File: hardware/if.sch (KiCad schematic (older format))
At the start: 59 parts, among them U34 ADA4940-2, U35 ADA4940-2

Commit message: Current working version.
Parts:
- C124, C125, C126, C127, C128, C129, C130, C131, C132, C133, C134, C135, C136, C137, C138, C139, C140, C141, C142, C143, C144, C145, C146, C147, C148, C149, C150, C151: footprint fmcw3:C_0402b -> Capacitor_SMD:C_0402_1005Metric; symbol C -> Device:C
- C173: footprint fmcw3:C_0805b -> Capacitor_SMD:C_0805_2012Metric; symbol C -> Device:C
- L10, L11, L8, L9: symbol INDUCTOR_SMALL -> Device:L
- R55, R56, R57, R58, R59, R60, R61, R62, R63, R64, R65, R66, R67, R68, R74, R75, R76, R77, R78, R86, R87, R89, R90, R94: symbol R -> Device:R
- U34, U35: symbol ADA4940-2 -> fmcw3-rescue:ADA4940-2
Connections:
- wire segments 164 -> 217

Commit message: Dropped the 3 from the end of the project name.
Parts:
- L10, L11, L8, L9: footprint fmcw3:C_0805b -> fmcw:C_0805b
- R55, R56, R57, R58, R59, R60, R61, R62, R63, R64, R65, R66, R67, R68, R74, R75, R76, R77, R78, R86, R87, R89, R90, R94: footprint fmcw3:R_0402b -> fmcw:R_0402b
- U34, U35: footprint fmcw3:VFQFN-24 -> fmcw:VFQFN-24; symbol fmcw3-rescue:ADA4940-2 -> fmcw-rescue:ADA4940-2-fmcw3-rescue
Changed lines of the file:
@@
 EESchema Schematic File Version 4
-LIBS:fmcw3-cache
+LIBS:fmcw-cache
 EELAYER 26 0
 EELAYER END
@@
 F 0 "L10" V 1790 1700 50  0000 C CNN
 F 1 "2.2u" V 1699 1700 50  0000 C CNN
-F 2 "fmcw3:C_0805b" H 1600 1700 60  0001 C CNN
+F 2 "fmcw:C_0805b" H 1600 1700 60  0001 C CNN
 F 3 "" H 1600 1700 60  0000 C CNN
 	1    1600 1700
@@
 F 0 "L11" V 1790 2100 50  0000 C CNN
 F 1 "2.2u" V 1699 2100 50  0000 C CNN
-F 2 "fmcw3:C_0805b" H 1600 2100 60  0001 C CNN
+F 2 "fmcw:C_0805b" H 1600 2100 60  0001 C CNN
 F 3 "" H 1600 2100 60  0000 C CNN
 	1    1600 2100
@@
 F 0 "R61" V 3980 1100 50  0000 C CNN
 F 1 "8.2k" V 3900 1100 50  0000 C CNN
-F 2 "fmcw3:R_0402b" V 3830 1100 30  0001 C CNN
+F 2 "fmcw:R_0402b" V 3830 1100 30  0001 C CNN
 F 3 "" H 3900 1100 30  0000 C CNN
 	1    3900 1100
@@
 F 0 "R62" V 3980 2600 50  0000 C CNN
 F 1 "8.2k" V 3900 2600 50  0000 C CNN
-F 2 "fmcw3:R_0402b" V 3830 2600 30  0001 C CNN
+F 2 "fmcw:R_0402b" V 3830 2600 30  0001 C CNN
 F 3 "" H 3900 2600 30  0000 C CNN
 	1    3900 2600
@@
 F 0 "R57" V 2980 1750 50  0000 C CNN
 F 1 "550" V 2900 1750 50  0000 C CNN
-F 2 "fmcw3:R_0402b" V 2830 1750 30  0001 C CNN
+F 2 "fmcw:R_0402b" V 2830 1750 30  0001 C CNN
 F 3 "" H 2900 1750 30  0000 C CNN
 	1    2900 1750
@@
 F 0 "R58" V 2980 2050 50  0000 C CNN
 F 1 "550" V 2900 2050 50  0000 C CNN
-F 2 "fmcw3:R_0402b" V 2830 2050 30  0001 C CNN
+F 2 "fmcw:R_0402b" V 2830 2050 30  0001 C CNN
 F 3 "" H 2900 2050 30  0000 C CNN
 	1    2900 2050
@@
 F 0 "L8" V 1590 4900 50  0000 C CNN
 F 1 "2.2u" V 1499 4900 50  0000 C CNN
-F 2 "fmcw3:C_0805b" H 1400 4900 60  0001 C CNN
+F 2 "fmcw:C_0805b" H 1400 4900 60  0001 C CNN
 F 3 "" H 1400 4900 60  0000 C CNN
 	1    1400 4900
@@
 F 0 "L9" V 1590 5300 50  0000 C CNN
 F 1 "2.2u" V 1499 5300 50  0000 C CNN
-F 2 "fmcw3:C_0805b" H 1400 5300 60  0001 C CNN
+F 2 "fmcw:C_0805b" H 1400 5300 60  0001 C CNN
 F 3 "" H 1400 5300 60  0000 C CNN
 	1    1400 5300
@@
 F 0 "R59" V 3780 4300 50  0000 C CNN
 F 1 "8.2k" V 3700 4300 50  0000 C CNN
-F 2 "fmcw3:R_0402b" V 3630 4300 30  0001 C CNN
+F 2 "fmcw:R_0402b" V 3630 4300 30  0001 C CNN
 F 3 "" H 3700 4300 30  0000 C CNN
 	1    3700 4300
@@
 F 0 "R60" V 3780 5800 50  0000 C CNN
 F 1 "8.2k" V 3700 5800 50  0000 C CNN
-F 2 "fmcw3:R_0402b" V 3630 5800 30  0001 C CNN
+F 2 "fmcw:R_0402b" V 3630 5800 30  0001 C CNN
 F 3 "" H 3700 5800 30  0000 C CNN
 	1    3700 5800
@@
 F 0 "R55" V 2780 4950 50  0000 C CNN
 F 1 "550" V 2700 4950 50  0000 C CNN
-F 2 "fmcw3:R_0402b" V 2630 4950 30  0001 C CNN
+F 2 "fmcw:R_0402b" V 2630 4950 30  0001 C CNN
 F 3 "" H 2700 4950 30  0000 C CNN
 	1    2700 4950
@@
 F 0 "R56" V 2780 5250 50  0000 C CNN
 F 1 "550" V 2700 5250 50  0000 C CNN
-F 2 "fmcw3:R_0402b" V 2630 5250 30  0001 C CNN
+F 2 "fmcw:R_0402b" V 2630 5250 30  0001 C CNN
 F 3 "" H 2700 5250 30  0000 C CNN
 	1    2700 5250
@@
 F 0 "R63" V 7180 1000 50  0000 C CNN
 F 1 "DNP" V 7100 1000 50  0000 C CNN
-F 2 "fmcw3:R_0402b" V 7030 1000 30  0001 C CNN
+F 2 "fmcw:R_0402b" V 7030 1000 30  0001 C CNN
 F 3 "" H 7100 1000 30  0000 C CNN
 	1    7100 1000
@@
 F 0 "R64" V 7180 2800 50  0000 C CNN
 F 1 "DNP" V 7100 2800 50  0000 C CNN
-F 2 "fmcw3:R_0402b" V 7030 2800 30  0001 C CNN
+F 2 "fmcw:R_0402b" V 7030 2800 30  0001 C CNN
 F 3 "" H 7100 2800 30  0000 C CNN
 	1    7100 2800
@@
 F 0 "R67" V 7830 1650 50  0000 C CNN
 F 1 "DNP" V 7750 1650 50  0000 C CNN
-F 2 "fmcw3:R_0402b" V 7680 1650 30  0001 C CNN
+F 2 "fmcw:R_0402b" V 7680 1650 30  0001 C CNN
 F 3 "" H 7750 1650 30  0000 C CNN
 	1    7750 1650
@@
 F 0 "R68" V 7830 2200 50  0000 C CNN
 F 1 "DNP" V 7750 2200 50  0000 C CNN
-F 2 "fmcw3:R_0402b" V 7680 2200 30  0001 C CNN
+F 2 "fmcw:R_0402b" V 7680 2200 30  0001 C CNN
 F 3 "" H 7750 2200 30  0000 C CNN
 	1    7750 2200
@@
 F 0 "R76" V 8280 1400 50  0000 C CNN
 F 1 "DNP" V 8200 1400 50  0000 C CNN
-F 2 "fmcw3:R_0402b" V 8130 1400 30  0001 C CNN
+F 2 "fmcw:R_0402b" V 8130 1400 30  0001 C CNN
 F 3 "" H 8200 1400 30  0000 C CNN
 	1    8200 1400
@@
 F 0 "R77" V 8280 2400 50  0000 C CNN
 F 1 "DNP" V 8200 2400 50  0000 C CNN
-F 2 "fmcw3:R_0402b" V 8130 2400 30  0001 C CNN
+F 2 "fmcw:R_0402b" V 8130 2400 30  0001 C CNN
 F 3 "" H 8200 2400 30  0000 C CNN
 	1    8200 2400
@@
 F 0 "R87" V 10330 1600 50  0000 C CNN
 F 1 "0" V 10250 1600 50  0000 C CNN
-F 2 "fmcw3:R_0402b" V 10180 1600 30  0001 C CNN
+F 2 "fmcw:R_0402b" V 10180 1600 30  0001 C CNN
 F 3 "" H 10250 1600 30  0000 C CNN
 	1    10250 1600
@@
 F 0 "R89" V 10330 2400 50  0000 C CNN
 F 1 "0" V 10250 2400 50  0000 C CNN
-F 2 "fmcw3:R_0402b" V 10180 2400 30  0001 C CNN
+F 2 "fmcw:R_0402b" V 10180 2400 30  0001 C CNN
 F 3 "" H 10250 2400 30  0000 C CNN
 	1    10250 2400
@@
 F 0 "R65" V 7180 4200 50  0000 C CNN
 F 1 "DNP" V 7100 4200 50  0000 C CNN
-F 2 "fmcw3:R_0402b" V 7030 4200 30  0001 C CNN
+F 2 "fmcw:R_0402b" V 7030 4200 30  0001 C CNN
 F 3 "" H 7100 4200 30  0000 C CNN
 	1    7100 4200
@@
 F 0 "R66" V 7180 6000 50  0000 C CNN
 F 1 "DNP" V 7100 6000 50  0000 C CNN
-F 2 "fmcw3:R_0402b" V 7030 6000 30  0001 C CNN
+F 2 "fmcw:R_0402b" V 7030 6000 30  0001 C CNN
 F 3 "" H 7100 6000 30  0000 C CNN
 	1    7100 6000
@@
 F 0 "R74" V 7830 4850 50  0000 C CNN
 F 1 "DNP" V 7750 4850 50  0000 C CNN
-F 2 "fmcw3:R_0402b" V 7680 4850 30  0001 C CNN
+F 2 "fmcw:R_0402b" V 7680 4850 30  0001 C CNN
 F 3 "" H 7750 4850 30  0000 C CNN
 	1    7750 4850
@@
 F 0 "R75" V 7830 5400 50  0000 C CNN
 F 1 "DNP" V 7750 5400 50  0000 C CNN
-F 2 "fmcw3:R_0402b" V 7680 5400 30  0001 C CNN
+F 2 "fmcw:R_0402b" V 7680 5400 30  0001 C CNN
 F 3 "" H 7750 5400 30  0000 C CNN
 	1    7750 5400
@@
 F 0 "R78" V 8280 4600 50  0000 C CNN
 F 1 "DNP" V 8200 4600 50  0000 C CNN
-F 2 "fmcw3:R_0402b" V 8130 4600 30  0001 C CNN
+F 2 "fmcw:R_0402b" V 8130 4600 30  0001 C CNN
 F 3 "" H 8200 4600 30  0000 C CNN
 	1    8200 4600
@@
 F 0 "R86" V 8280 5600 50  0000 C CNN
 F 1 "DNP" V 8200 5600 50  0000 C CNN
-F 2 "fmcw3:R_0402b" V 8130 5600 30  0001 C CNN
+F 2 "fmcw:R_0402b" V 8130 5600 30  0001 C CNN
 F 3 "" H 8200 5600 30  0000 C CNN
 	1    8200 5600
@@
 F 0 "R90" V 10330 4800 50  0000 C CNN
 F 1 "0" V 10250 4800 50  0000 C CNN
-F 2 "fmcw3:R_0402b" V 10180 4800 30  0001 C CNN
+F 2 "fmcw:R_0402b" V 10180 4800 30  0001 C CNN
 F 3 "" H 10250 4800 30  0000 C CNN
 	1    10250 4800
@@
 F 0 "R94" V 10330 5600 50  0000 C CNN
 F 1 "0" V 10250 5600 50  0000 C CNN
-F 2 "fmcw3:R_0402b" V 10180 5600 30  0001 C CNN
+F 2 "fmcw:R_0402b" V 10180 5600 30  0001 C CNN
 F 3 "" H 10250 5600 30  0000 C CNN
 	1    10250 5600
@@
 $EndComp
 $Comp
-L fmcw3-rescue:ADA4940-2 U34
+L fmcw-rescue:ADA4940-2-fmcw3-rescue U34
 U 1 1 59758BEE
 P 4700 1900
@@
 F 0 "U34" H 5100 1500 60  0000 C CNN
 F 1 "ADA4940-2" H 5050 2300 60  0000 C CNN
-F 2 "fmcw3:VFQFN-24" H 4750 1900 60  0001 C CNN
+F 2 "fmcw:VFQFN-24" H 4750 1900 60  0001 C CNN
 F 3 "" H 4750 1900 60  0001 C CNN
 	1    4700 1900
@@
 $EndComp
 $Comp
-L fmcw3-rescue:ADA4940-2 U35
+L fmcw-rescue:ADA4940-2-fmcw3-rescue U35
 U 1 1 59758D01
 P 9250 1950
@@
 F 0 "U35" H 9650 1550 60  0000 C CNN
 F 1 "ADA4940-2" H 9600 2350 60  0000 C CNN
-F 2 "fmcw3:VFQFN-24" H 9300 1950 60  0001 C CNN
+F 2 "fmcw:VFQFN-24" H 9300 1950 60  0001 C CNN
 F 3 "http://www.analog.com/media/en/technical-documentation/data-sheets/ADA4940-1_4940-2.pdf" H 9300 1950 60  0001 C CNN
 	1    9250 1950
@@
 $EndComp
 $Comp
-L fmcw3-rescue:ADA4940-2 U34
+L fmcw-rescue:ADA4940-2-fmcw3-rescue U34
 U 2 1 59758E37
 P 4500 5100
@@
 F 0 "U34" H 4900 4700 60  0000 C CNN
 F 1 "ADA4940-2" H 4850 5500 60  0000 C CNN
-F 2 "fmcw3:VFQFN-24" H 4550 5100 60  0001 C CNN
+F 2 "fmcw:VFQFN-24" H 4550 5100 60  0001 C CNN
 F 3 "" H 4550 5100 60  0001 C CNN
 	2    4500 5100
@@
 $EndComp
 $Comp
-L fmcw3-rescue:ADA4940-2 U35
+L fmcw-rescue:ADA4940-2-fmcw3-rescue U35
 U 2 1 59758F37
 P 9250 5150
@@
 F 0 "U35" H 9650 4750 60  0000 C CNN
 F 1 "ADA4940-2" H 9600 5550 60  0000 C CNN
-F 2 "fmcw3:VFQFN-24" H 9300 5150 60  0001 C CNN
+F 2 "fmcw:VFQFN-24" H 9300 5150 60  0001 C CNN
 F 3 "http://www.analog.com/media/en/technical-documentation/data-sheets/ADA4940-1_4940-2.pdf" H 9300 5150 60  0001 C CNN
 	2    9250 5150

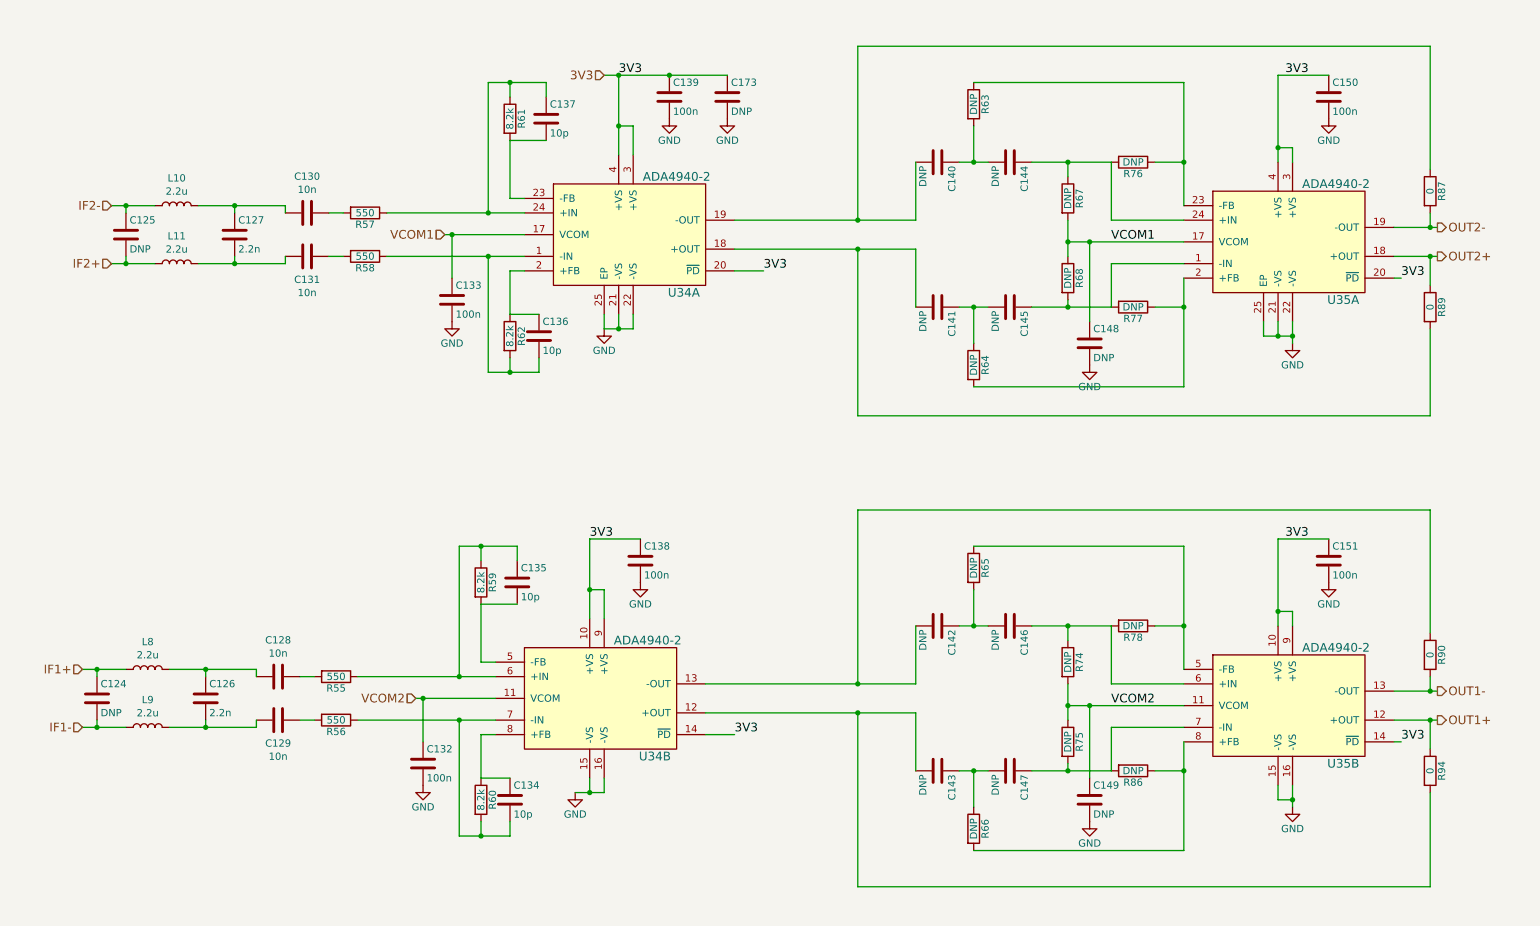
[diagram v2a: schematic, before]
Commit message: Improved top level documentation.
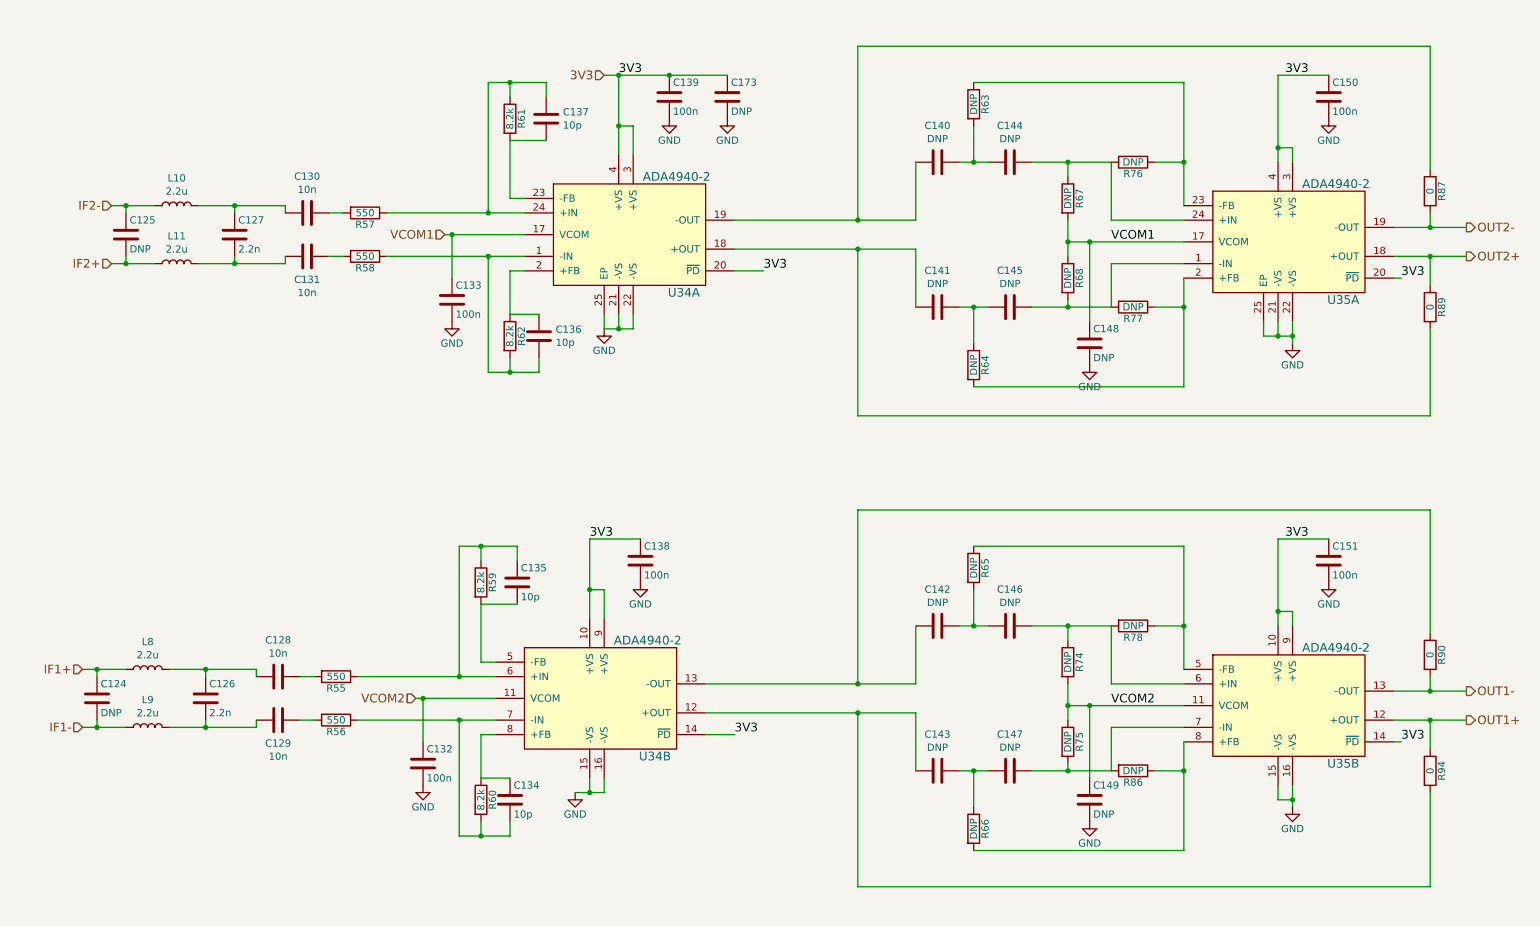
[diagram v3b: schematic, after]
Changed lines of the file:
@@
 U 1 1 59668634
 P 4100 2600
-F 0 "C136" H 4125 2700 50  0000 L CNN
-F 1 "10p" H 4125 2500 50  0000 L CNN
+F 0 "C136" H 4215 2646 50  0000 L CNN
+F 1 "10p" H 4215 2555 50  0000 L CNN
 F 2 "Capacitor_SMD:C_0402_1005Metric" H 4138 2450 30  0001 C CNN
 F 3 "" H 4100 2600 60  0000 C CNN
@@
 U 1 1 59668714
 P 4150 1100
-F 0 "C137" H 4175 1200 50  0000 L CNN
-F 1 "10p" H 4175 1000 50  0000 L CNN
+F 0 "C137" H 4265 1146 50  0000 L CNN
+F 1 "10p" H 4265 1055 50  0000 L CNN
 F 2 "Capacitor_SMD:C_0402_1005Metric" H 4188 950 30  0001 C CNN
 F 3 "" H 4150 1100 60  0000 C CNN
@@
 U 1 1 5966D17D
 P 6850 1400
-F 0 "C140" H 6875 1500 50  0000 L CNN
-F 1 "DNP" H 6875 1300 50  0000 L CNN
+F 0 "C140" V 6598 1400 50  0000 C CNN
+F 1 "DNP" V 6689 1400 50  0000 C CNN
 F 2 "Capacitor_SMD:C_0402_1005Metric" H 6888 1250 30  0001 C CNN
 F 3 "" H 6850 1400 60  0000 C CNN
@@
 U 1 1 5966D1F5
 P 7350 1400
-F 0 "C144" H 7375 1500 50  0000 L CNN
-F 1 "DNP" H 7375 1300 50  0000 L CNN
+F 0 "C144" V 7098 1400 50  0000 C CNN
+F 1 "DNP" V 7189 1400 50  0000 C CNN
 F 2 "Capacitor_SMD:C_0402_1005Metric" H 7388 1250 30  0001 C CNN
 F 3 "" H 7350 1400 60  0000 C CNN
@@
 U 1 1 5966D451
 P 6850 2400
-F 0 "C141" H 6875 2500 50  0000 L CNN
-F 1 "DNP" H 6875 2300 50  0000 L CNN
+F 0 "C141" V 6598 2400 50  0000 C CNN
+F 1 "DNP" V 6689 2400 50  0000 C CNN
 F 2 "Capacitor_SMD:C_0402_1005Metric" H 6888 2250 30  0001 C CNN
 F 3 "" H 6850 2400 60  0000 C CNN
@@
 U 1 1 5966D457
 P 7350 2400
-F 0 "C145" H 7375 2500 50  0000 L CNN
-F 1 "DNP" H 7375 2300 50  0000 L CNN
+F 0 "C145" V 7098 2400 50  0000 C CNN
+F 1 "DNP" V 7189 2400 50  0000 C CNN
 F 2 "Capacitor_SMD:C_0402_1005Metric" H 7388 2250 30  0001 C CNN
 F 3 "" H 7350 2400 60  0000 C CNN
@@
 	0    1    1    0
 $EndComp
-Text HLabel 10300 5250 2    60   Output ~ 0
+Text HLabel 10500 5250 2    60   Output ~ 0
 OUT1+
-Text HLabel 10300 5050 2    60   Output ~ 0
+Text HLabel 10500 5050 2    60   Output ~ 0
 OUT1-
 $Comp
@@
 U 1 1 596760CC
 P 6850 4600
-F 0 "C142" H 6875 4700 50  0000 L CNN
-F 1 "DNP" H 6875 4500 50  0000 L CNN
+F 0 "C142" V 6598 4600 50  0000 C CNN
+F 1 "DNP" V 6689 4600 50  0000 C CNN
 F 2 "Capacitor_SMD:C_0402_1005Metric" H 6888 4450 30  0001 C CNN
 F 3 "" H 6850 4600 60  0000 C CNN
@@
 U 1 1 596760D2
 P 7350 4600
-F 0 "C146" H 7375 4700 50  0000 L CNN
-F 1 "DNP" H 7375 4500 50  0000 L CNN
+F 0 "C146" V 7098 4600 50  0000 C CNN
+F 1 "DNP" V 7189 4600 50  0000 C CNN
 F 2 "Capacitor_SMD:C_0402_1005Metric" H 7388 4450 30  0001 C CNN
 F 3 "" H 7350 4600 60  0000 C CNN
@@
 U 1 1 596760D8
 P 6850 5600
-F 0 "C143" H 6875 5700 50  0000 L CNN
-F 1 "DNP" H 6875 5500 50  0000 L CNN
+F 0 "C143" V 6598 5600 50  0000 C CNN
+F 1 "DNP" V 6689 5600 50  0000 C CNN
 F 2 "Capacitor_SMD:C_0402_1005Metric" H 6888 5450 30  0001 C CNN
 F 3 "" H 6850 5600 60  0000 C CNN
@@
 U 1 1 596760DE
 P 7350 5600
-F 0 "C147" H 7375 5700 50  0000 L CNN
-F 1 "DNP" H 7375 5500 50  0000 L CNN
+F 0 "C147" V 7098 5600 50  0000 C CNN
+F 1 "DNP" V 7189 5600 50  0000 C CNN
 F 2 "Capacitor_SMD:C_0402_1005Metric" H 7388 5450 30  0001 C CNN
 F 3 "" H 7350 5600 60  0000 C CNN
@@
 	0    1    1    0
 $EndComp
-Text HLabel 10300 2050 2    60   Output ~ 0
+Text HLabel 10500 2050 2    60   Output ~ 0
 OUT2+
-Text HLabel 10300 1850 2    60   Output ~ 0
+Text HLabel 10500 1850 2    60   Output ~ 0
 OUT2-
 $Comp
@@
 	8550 1400 8550 1700
 Wire Wire Line
-	10250 1850 10300 1850
-Wire Wire Line
-	10250 2050 10300 2050
+	10250 1850 10500 1850
+Wire Wire Line
+	10250 2050 10500 2050
 Wire Wire Line
 	6300 2000 6700 2000
@@
 	8550 4600 8550 4900
 Wire Wire Line
-	10250 5050 10300 5050
-Wire Wire Line
-	10250 5250 10300 5250
+	10250 5050 10500 5050
+Wire Wire Line
+	10250 5250 10500 5250
 Wire Wire Line
 	6300 5200 6700 5200
